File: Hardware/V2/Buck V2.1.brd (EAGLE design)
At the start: 99.8 x 99.8 mm, 122 parts, among them Q1 IRF3205STRLPBF, Q2 IRF3205STRLPBF, Q3 IRF3205STRLPBF, Q4 IRF3205STRLPBF, Q5 IRF3205STRLPBF, Q6 IRF3205STRLPBF, Q7 IRF3205STRLPBF, Q8 IRF3205STRLPBF, SW1 PTR1TP20R, U1 Value, U2 Value

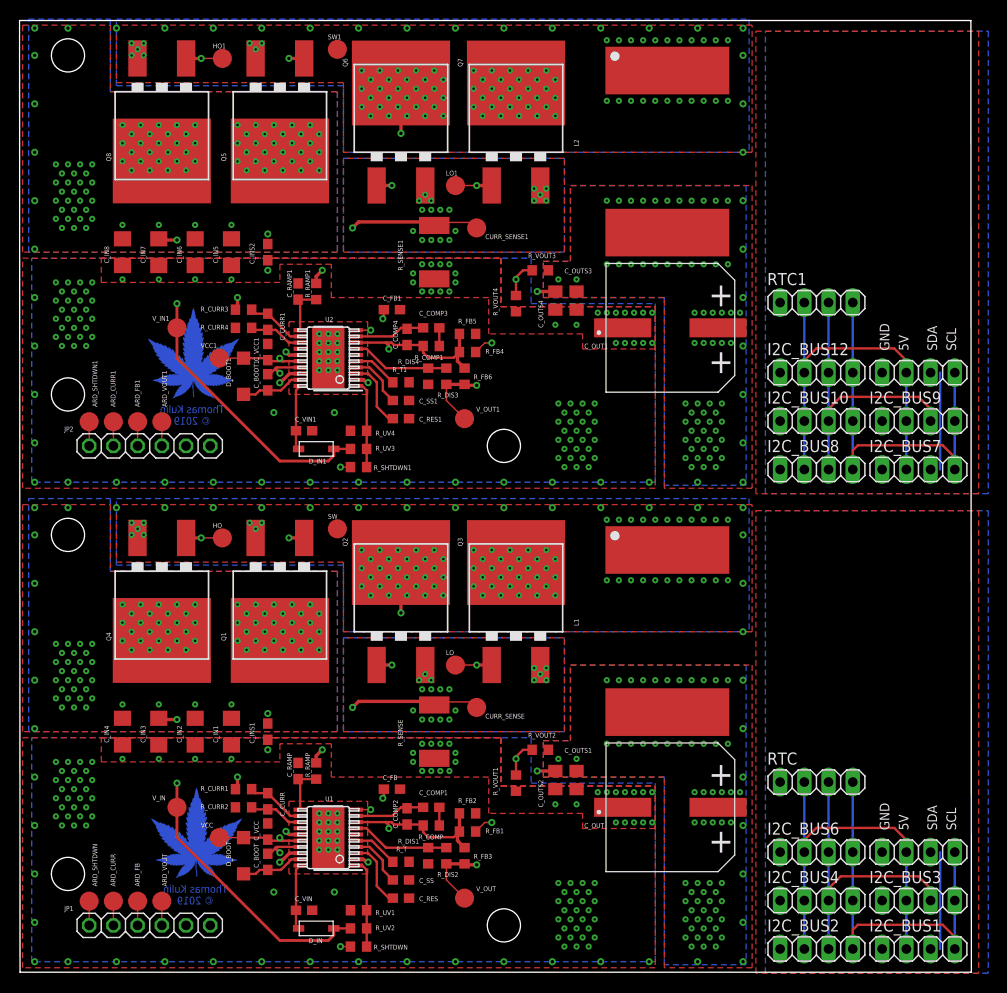
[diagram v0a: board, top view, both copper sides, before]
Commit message: updated buck v2.1 to reflect actual boards ordered from JLC
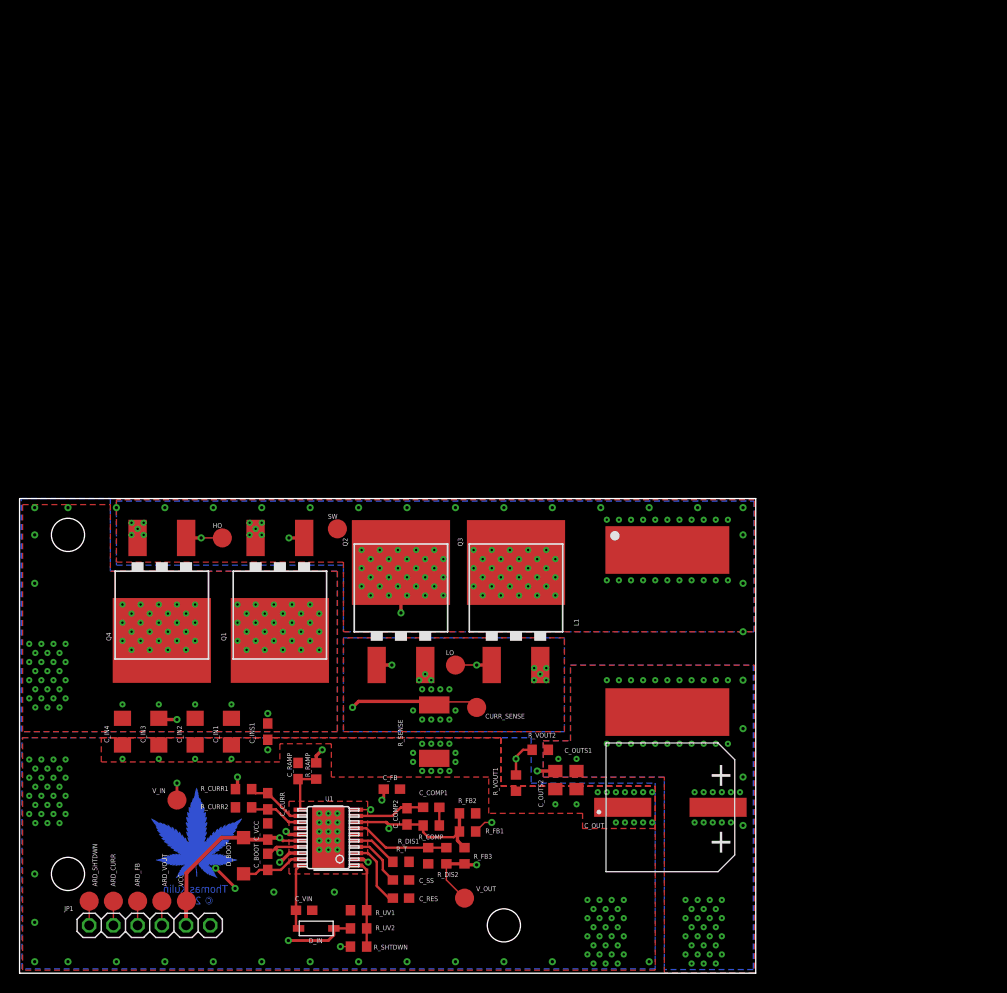
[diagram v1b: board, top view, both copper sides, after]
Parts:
- removed ARD_CURR1, ARD_FB1, ARD_SHTDWN1, ARD_VOUT1, CURR_SENSE1, HO1, LO1, SW1, VCC1, V_IN1, V_OUT1: PTR1TP20R, testpad:TP20R
- removed C_BOOT1: 470 nF 50V, rcl:C0603
- removed C_COMP3: 1.2 nF, rcl:C0603
- removed C_COMP4: 82 pF, rcl:C0603
- removed C_CURR1: 100 pF, rcl:C0603
- removed C_FB1: 0.68 uF, rcl:C0603
- removed C_IN5, C_IN6, C_IN7, C_IN8: 10 uF, rcl:C1206
- removed C_INS2, C_SS1: 100 nF, rcl:C0603
- removed C_OUT1: 470 uF, custom-parts:CAP_PANASONIC_H13
- removed C_OUTS3, C_OUTS4: 1 uF, rcl:C0805
- removed C_RAMP1: 820pF 50V, rcl:C0603
- removed C_RES1: 1 uF, rcl:C0603
- removed C_VCC1, C_VIN1: 1 UF, rcl:C0603
- removed D_BOOT1: PMEG10010ELRX, diode:SOD123
- removed D_IN1: IN4148, adafruit:SOD-123
- removed I2C_BUS1, I2C_BUS10, I2C_BUS11, I2C_BUS12, I2C_BUS2, I2C_BUS3, I2C_BUS4, I2C_BUS5, I2C_BUS6, I2C_BUS7, I2C_BUS8, I2C_BUS9, RTC, RTC1: (no value), pinhead:1X04
- removed JP2: (no value), adafruit:1X06
- removed L2: (no value), custom-parts:17.5X17.5_INDUCTOR_SMD
- removed Q5, Q6, Q7, Q8: IRF3205STRLPBF, mixed_components:D2PAK
- removed R_COMP1: 28.7 K, rcl:R0603
- removed R_CURR3, R_CURR4: 100, rcl:R0603
- removed R_DIS3, R_UV3: 56 K, rcl:R0603
- removed R_DIS4, R_UV4: 3.3 K, rcl:R0603
- removed R_FB4: 17 K, rcl:R0603
- removed R_FB5: 10 K, rcl:R0603
- removed R_FB6: 178 K, rcl:R0603
- removed R_RAMP1: 180 KOhm, rcl:R0603
- removed R_SENSE1: 1W 5mOhm, rcl:R2512
- removed R_SHTDWN1, R_VOUT4: 1 K, rcl:R0603
- removed R_T1: 12.1 K, rcl:R0603
- removed R_VOUT3: 5 K, rcl:R0603
- removed U2: Value, AcceleratedDesigns_Lib:PWP0020A
- moved VCC 7.50 mm to (17.5, 7.57)
- moved V_IN 0.76 mm to (16.5, 18.2)
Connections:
- removed net 5V: I2C_BUS1.2, I2C_BUS2.2, I2C_BUS3.2, I2C_BUS4.2, I2C_BUS5.2, I2C_BUS6.2, RTC.2
- removed net 5V1: I2C_BUS10.2, I2C_BUS11.2, I2C_BUS12.2, I2C_BUS7.2, I2C_BUS8.2, I2C_BUS9.2, RTC1.2
- removed net ARD_CURRENT1: ARD_CURR1.TP, JP2.2, U2.10
- removed net ARD_FEEDBACK1: ARD_FB1.TP, JP2.3, R_FB4.1
- removed net ARD_SHUTDOWN1: ARD_SHTDWN1.TP, JP2.1, R_SHTDWN1.1
- removed net ARD_VOUT1: ARD_VOUT1.TP, JP2.4, R_VOUT3.1, R_VOUT4.2
- removed net GND1: C_FB1.2, C_IN5.2, C_IN6.2, C_IN7.2, C_IN8.2, C_INS2.2, C_OUT1.P$1, C_OUTS3.2, C_OUTS4.2, C_RAMP1.2, C_RES1.2, C_SS1.2, C_VCC1.2, C_VIN1.2, JP2.5, JP2.6, R_CURR4.2, R_DIS4.2, R_FB5.1, R_SENSE1.2, R_T1.1, R_UV4.2, R_VOUT4.1, U2.14, U2.21, U2.6
- removed net GND2: I2C_BUS1.1, I2C_BUS2.1, I2C_BUS3.1, I2C_BUS4.1, I2C_BUS5.1, I2C_BUS6.1, RTC.1
- removed net GND3: I2C_BUS10.1, I2C_BUS11.1, I2C_BUS12.1, I2C_BUS7.1, I2C_BUS8.1, I2C_BUS9.1, RTC1.1
- removed net N$1: C_VCC.1, D_BOOT.A, U1.16, U1.2, VCC.TP
- removed net N$12: C_BOOT1.1, D_BOOT1.C, U2.19
- removed net N$22: C_BOOT1.2, L2.1, Q5.3, Q6.2, Q7.2, Q8.3, R_RAMP1.2, SW1.TP, U2.17
- removed net N$23: CURR_SENSE1.TP, Q6.3, Q7.3, R_CURR3.2, R_SENSE1.1
- removed net N$24: C_RAMP1.1, R_RAMP1.1, U2.11
- removed net N$25: LO1.TP, Q6.1, Q7.1, U2.15
- removed net N$26: HO1.TP, Q5.1, Q8.1, U2.18
- removed net N$27: R_SHTDWN1.2, R_UV3.1, R_UV4.1, U2.1
- removed net N$28: R_DIS3.1, R_DIS4.1, U2.7
- removed net N$29: C_COMP3.2, R_COMP1.2
- removed net N$30: C_COMP3.1, C_COMP4.1, U2.9
- removed net N$31: C_COMP4.2, C_FB1.1, R_COMP1.1, R_FB4.2, R_FB5.2, R_FB6.1, U2.8
- removed net N$32: R_T1.2, U2.5
- removed net N$33: C_SS1.1, U2.4
- removed net N$34: C_RES1.1, U2.3
- removed net N$35: C_CURR1.1, R_CURR3.1, U2.12
- removed net N$36: C_CURR1.2, R_CURR4.1, U2.13
- removed net N$37: C_VIN1.1, D_IN1.C, U2.20
- removed net N$38: C_IN5.1, C_IN6.1, C_IN7.1, C_IN8.1, C_INS2.1, D_IN1.A, Q5.2, Q8.2, R_UV3.2, V_IN1.TP
- removed net N$6: C_VCC1.1, D_BOOT1.A, U2.16, U2.2, VCC1.TP
- removed net SCL: I2C_BUS1.4, I2C_BUS2.4, I2C_BUS3.4, I2C_BUS4.4, I2C_BUS5.4, I2C_BUS6.4, RTC.4
- removed net SCL1: I2C_BUS10.4, I2C_BUS11.4, I2C_BUS12.4, I2C_BUS7.4, I2C_BUS8.4, I2C_BUS9.4, RTC1.4
- removed net SDA: I2C_BUS1.3, I2C_BUS2.3, I2C_BUS3.3, I2C_BUS4.3, I2C_BUS5.3, I2C_BUS6.3, RTC.3
- removed net SDA1: I2C_BUS10.3, I2C_BUS11.3, I2C_BUS12.3, I2C_BUS7.3, I2C_BUS8.3, I2C_BUS9.3, RTC1.3
- removed net V_OUT1: C_OUT1.P$2, C_OUTS3.1, C_OUTS4.1, L2.2, R_DIS3.2, R_FB6.2, R_VOUT3.2, V_OUT1.TP
- new net VCC: C_VCC.1, D_BOOT.A, JP1.5, U1.16, U1.2, VCC.TP
- net GND: no longer JP1.5
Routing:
- net ARD_VOUT1: track 56.7 -> 0.00 mm, vias 1 -> 0
- net N$26: track 55.3 -> 0.00 mm, vias 3 -> 0
- net ARD_FEEDBACK1: track 49.1 -> 0.00 mm, vias 1 -> 0
- net N$22: track 44.8 -> 0.00 mm, vias 93 -> 0
- net ARD_CURRENT1: track 43.0 -> 0.00 mm, vias 1 -> 0
- net SCL1: track 42.4 -> 0.00 mm
- net SCL: track 42.4 -> 0.00 mm
- net 5V: track 42.0 -> 0.00 mm
- net SDA: track 42.0 -> 0.00 mm
- net 5V1: track 42.0 -> 0.00 mm
- net SDA1: track 42.0 -> 0.00 mm
- net N$25: track 38.2 -> 0.00 mm, vias 3 -> 0
- net N$38: track 37.9 -> 0.00 mm, vias 92 -> 0
- net VCC: track 0.00 -> 31.6 mm, vias 0 -> 2
- net ARD_SHUTDOWN1: track 31.4 -> 0.00 mm, vias 1 -> 0
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- removed copper zone on layer 1, net GND1
- removed copper zone on layer 15, net GND1
- removed copper zone on layer 16, net GND1
- removed copper zone on layer 2, net GND1
- removed copper zone on layer 1, net GND2
- removed copper zone on layer 15, net GND2
- removed copper zone on layer 16, net GND2
- removed copper zone on layer 2, net GND2
- removed copper zone on layer 1, net GND3
- removed copper zone on layer 15, net GND3
- removed copper zone on layer 16, net GND3
- removed copper zone on layer 2, net GND3
- removed copper zone on layer 1, net N$22
- removed copper zone on layer 16, net N$22
- removed copper zone on layer 1, net N$23
- removed copper zone on layer 16, net N$23
- removed copper zone on layer 1, net N$38
- removed copper zone on layer 16, net N$38
- removed copper zone on layer 1, net V_OUT1
- removed copper zone on layer 16, net V_OUT1
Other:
- board size 99.8 x 99.8 mm -> 77.2 x 49.8 mm
- board text removed: "5V"
- board text removed: "GND"
- board text removed: "I2C_BUS1"
- board text removed: "I2C_BUS2"
- board text removed: "I2C_BUS3"
- board text removed: "I2C_BUS4"
- board text removed: "I2C_BUS6"
- board text removed: "RTC"
- board text removed: "SCL"
- board text removed: "SDA"
- board text removed: "V Score"
